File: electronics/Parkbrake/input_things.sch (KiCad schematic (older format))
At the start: 14 parts, among them Q31 BSS138, U27 SN74LVC245ADBR

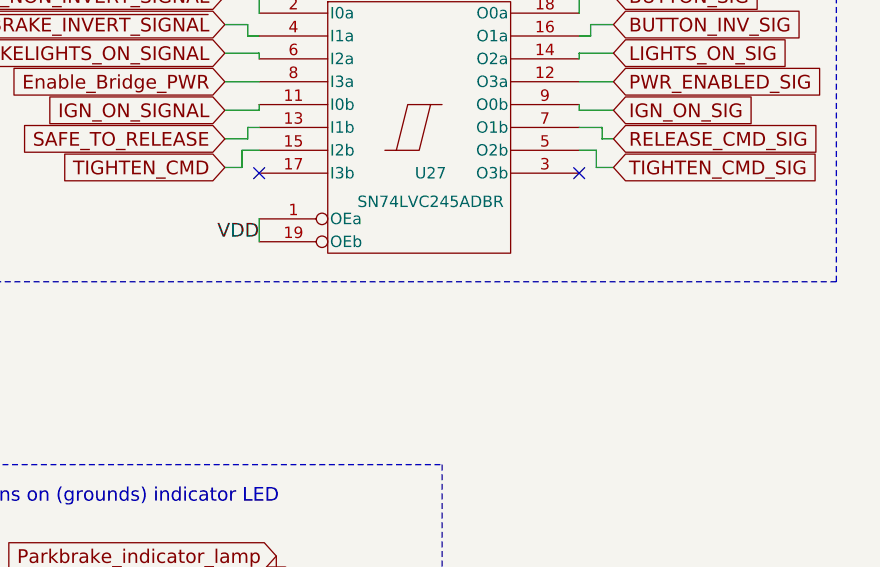
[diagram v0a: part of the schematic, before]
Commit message: Wrong IC
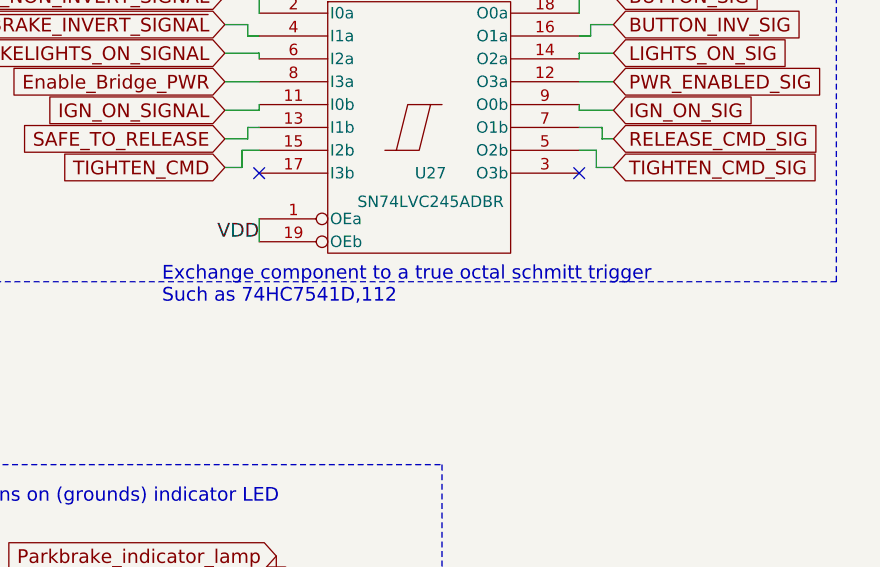
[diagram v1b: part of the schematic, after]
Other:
- note added: "Exchange component to a true octal schmitt trigger\nSuch as 74HC7541D,112"
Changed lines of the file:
@@
 $EndComp
 $Comp
-L GND #PWR85
+L GND #PWR092
 U 1 1 5793D9FE
 P 8400 2000
-F 0 "#PWR85" H 8400 1750 50  0001 C CNN
+F 0 "#PWR092" H 8400 1750 50  0001 C CNN
 F 1 "GND" H 8400 1850 50  0001 C CNN
 F 2 "" H 8400 2000 50  0000 C CNN
@@
 +12V_powerFront
 $Comp
-L GND #PWR83
+L GND #PWR093
 U 1 1 5793F3F6
 P 2625 3025
-F 0 "#PWR83" H 2625 2775 50  0001 C CNN
+F 0 "#PWR093" H 2625 2775 50  0001 C CNN
 F 1 "GND" H 2625 2875 50  0000 C CNN
 F 2 "" H 2625 3025 50  0000 C CNN
@@
 +12V_feed
 $Comp
-L GND #PWR82
+L GND #PWR094
 U 1 1 57945BF9
 P 2600 5425
-F 0 "#PWR82" H 2600 5175 50  0001 C CNN
+F 0 "#PWR094" H 2600 5175 50  0001 C CNN
 F 1 "GND" H 2600 5275 50  0000 C CNN
 F 2 "" H 2600 5425 50  0000 C CNN
@@
 $EndComp
 $Comp
-L GND #PWR84
+L GND #PWR095
 U 1 1 57942417
 P 7725 5375
-F 0 "#PWR84" H 7725 5125 50  0001 C CNN
+F 0 "#PWR095" H 7725 5125 50  0001 C CNN
 F 1 "GND" H 7725 5225 50  0000 C CNN
 F 2 "" H 7725 5375 50  0000 C CNN
@@
 Text Notes 6375 5475 0    60   ~ 0
 Diode is for ESD protection
+Text Notes 7225 3575 0    60   ~ 0
+Exchange component to a true octal schmitt trigger\nSuch as 74HC7541D,112
 $EndSCHEMATC
